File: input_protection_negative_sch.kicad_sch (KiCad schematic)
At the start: 23 parts, among them Q4 SQM50020EL, Q6 SQM50020EL, Q7 MMBT3904

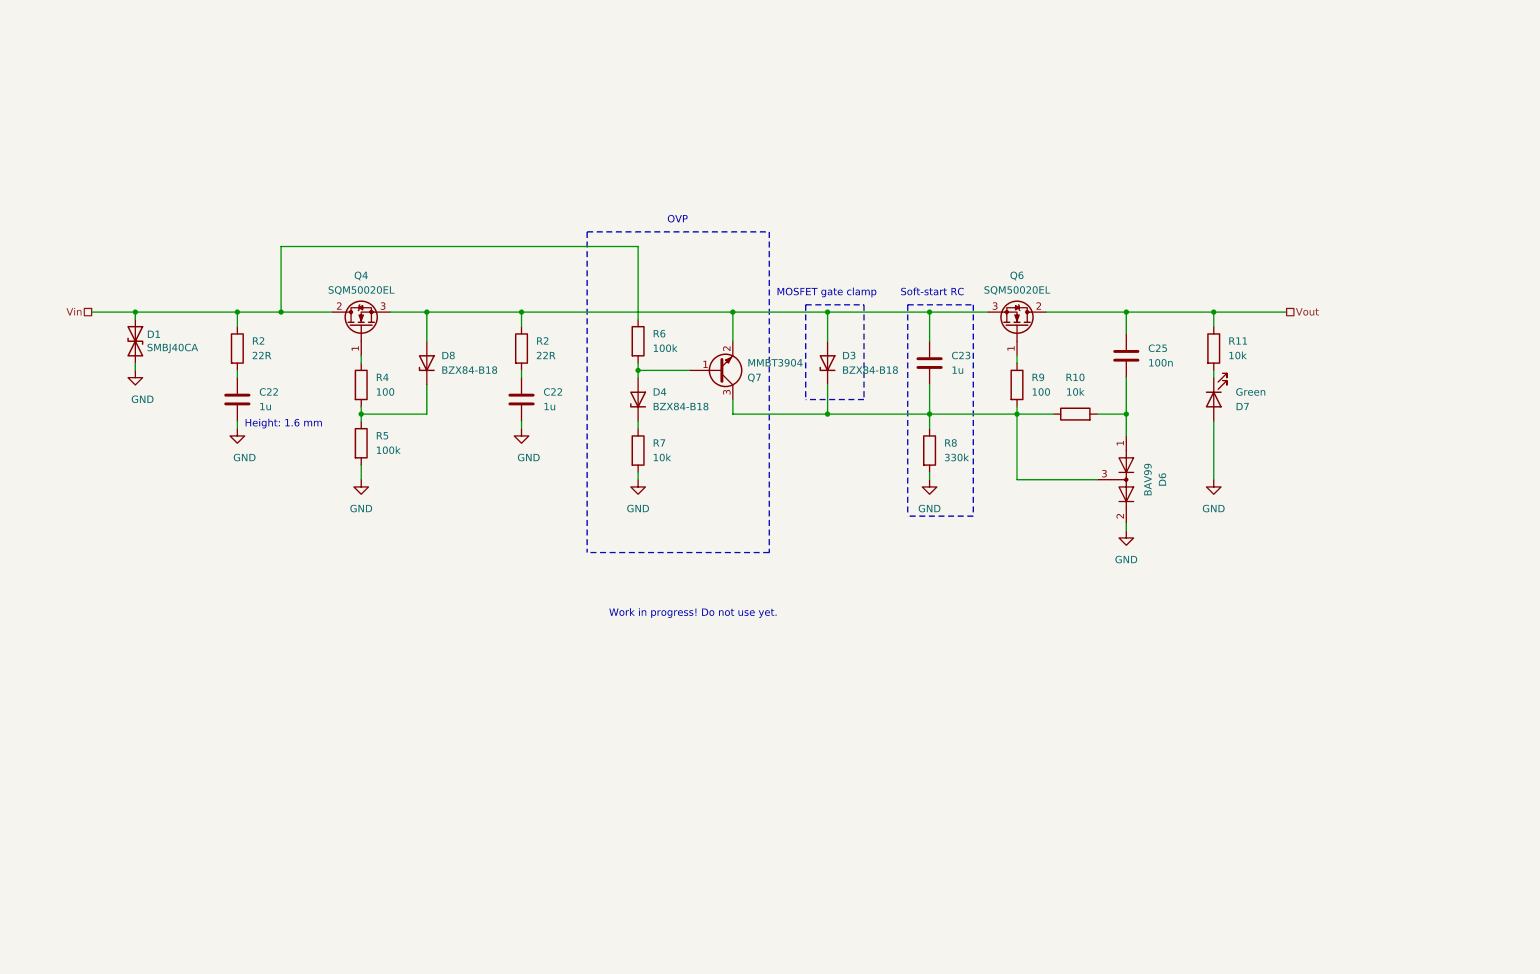
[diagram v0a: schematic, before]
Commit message: Added an input protection circuit Added CI
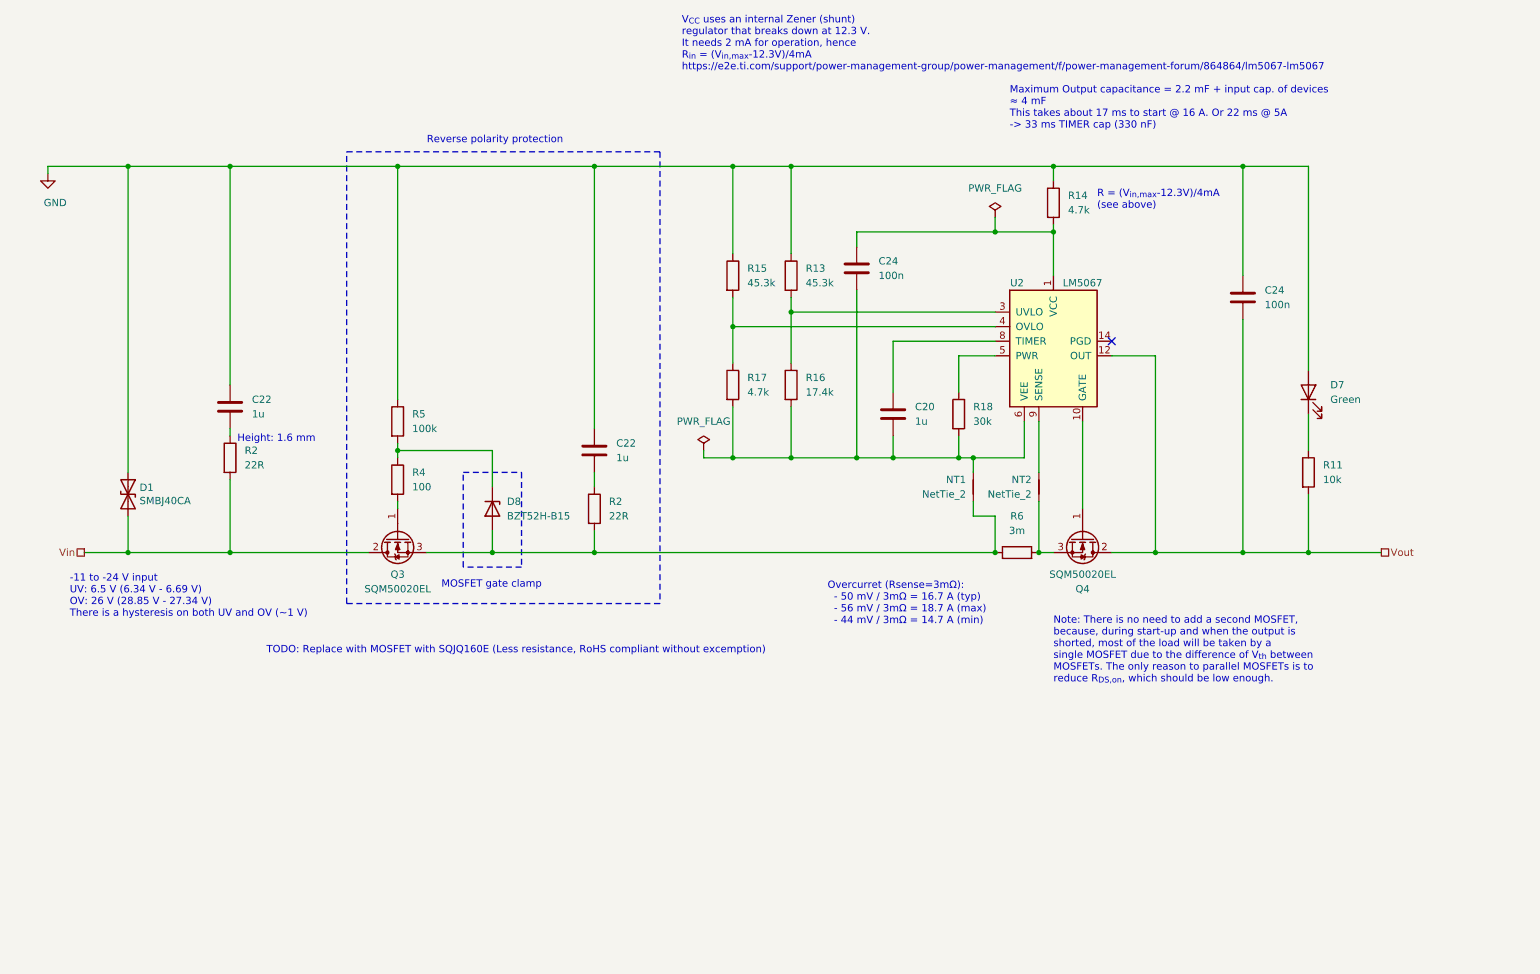
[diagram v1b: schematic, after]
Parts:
- removed C23: 1u, Capacitor_SMD:C_1206_3216Metric, symbol Device:C
- removed C25: 100n, Capacitor_SMD:C_1206_3216Metric, symbol Device:C
- removed D3, D4: BZX84-B18, Package_TO_SOT_SMD:SOT-23, symbol Diode:BZX84Cxx
- removed D6: BAV99, Package_TO_SOT_SMD:SOT-23, symbol Diode:BAV99
- removed Q7: MMBT3904, Package_TO_SOT_SMD:SOT-23, symbol Transistor_BJT:MMBT3904
- removed R10, R7: 10k, Resistor_SMD:R_0805_2012Metric, symbol Device:R
- removed R8: 330k, Resistor_SMD:R_0805_2012Metric, symbol Device:R
- removed R9: 100, Resistor_SMD:R_0805_2012Metric, symbol Device:R
- added C20: 1u, Capacitor_SMD:C_1206_3216Metric, symbol Device:C
- added C24 (x2): 100n, Capacitor_SMD:C_0805_2012Metric, symbol Device:C
- added NT1: NetTie_2, NetTie:NetTie-2_SMD_Pad0.5mm, symbol Device:NetTie_2
- added NT2: NetTie_2, Custom_footprints:NET-TIE-0.20mm, symbol Device:NetTie_2
- added R13, R15: 45.3k, Resistor_SMD:R_0805_2012Metric, symbol Device:R
- added R14, R17: 4.7k, Resistor_SMD:R_0805_2012Metric, symbol Device:R
- added R16: 17.4k, Resistor_SMD:R_0805_2012Metric, symbol Device:R
- added R18: 30k, Resistor_SMD:R_0805_2012Metric, symbol Device:R
- added U2: LM5067, Package_SO:SOIC-14_3.9x8.7mm_P1.27mm, symbol Texas Instruments:LM5067
- C22: RoHS (none) -> Yes; Temperature (none) -> Tstorage = –55 °C to 155 °C; digikey# (none) -> 399-13374-1-ND
- D1: MFN Bourns -> Littlefuse; PN SMBJ40CA-QH -> SZ1SMB40CAT3G; RoHS (none) -> Yes; Temperature (none) -> Tstorage = –55 °C to 150 °C
- D7: MFN Kingbright -> Osram; PN APT1608SGC -> LG L29K-G2J1-24; RoHS (none) -> Yes; Temperature (none) -> Tstorage = –40 °C to 100 °C
- D8: value BZX84-B18 -> BZT52H-B15; footprint Package_TO_SOT_SMD:SOT-23 -> Diode_SMD:D_SOD-123F; symbol Diode:BZX84Cxx -> Diode:BZT52Bxx; PN BZX84-B18,215 -> BZT52H-B15\,115; RoHS (none) -> Yes; Temperature (none) -> Tstorage = –65 °C to 150 °C; digikey# (none) -> 1727-1598-1-ND
- Q3: renamed from Q4; Note (none) -> Vds >= 60V; RoHS (none) -> By exemption; Temperature (none) -> Tstorage = –75 °C to 175 °C
- Q4: renamed from Q6; Note (none) -> Vds >= 60V; RoHS (none) -> By exemption; Temperature (none) -> Tstorage = –75 °C to 175 °C
- R11, R4, R5: Note (none) -> 1%, 150 V; RoHS (none) -> By exemption; Temperature (none) -> Tstorage = –55 °C to 155 °C
- R2: RoHS (none) -> By exemption; Temperature (none) -> Tstorage = –55 °C to 155 °C
- R6: value 100k -> 3m; footprint Resistor_SMD:R_0805_2012Metric -> Resistor_SMD:R_2512_6332Metric; MFN Vishay -> Bourns; PN CRCW0805100KFKEA -> CRE2512-FZ-R003E-3; RoHS (none) -> By exemption; Temperature (none) -> Tstorage = –75 °C to 170 °C
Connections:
- net GND: now also C22.1, C22.1, D1.1 (A1), R5.1, C24.1, R13.1, R14.1, R15.1; no longer C22.2, C22.2, D1.2 (A2), R5.2
- net Vin: now also D1.2 (A2), R2.2; no longer D1.1 (A1), R2.1, R6.1
- net Vout: now also R11.2, C24.2, U2.12 (OUT); no longer R11.1
- net at Q4.1 (G): now also U2.10 (GATE)
- net at D8.2 (A): now also Q3.3 (S), R2.2, R6.1, NT1.1
- net at R6.2: now also Q4.3 (S), NT2.1
- net at R4.1: now also D8.1 (K), R5.2; no longer Q3.1 (G)
- net at D7.1 (K): now also R11.1; no longer R11.2
- new net: C22.2, R2.1 (x2)
- new net: R13.2, R16.1, U2.3 (UVLO)
- new net: C20.2, C24.2, NT1.2, R16.2, R17.2, R18.2, U2.6 (VEE)
- new net: R15.2, R17.1, U2.4 (OVLO)
- new net: C24.1, R14.2, U2.1 (VCC)
- new net: R18.1, U2.5 (PWR)
- new net: C20.1, U2.8 (TIMER)
- new net: NT2.2, U2.9 (SENSE)
- new net: Q3.1 (G), R4.2
- no-connect marks 0 -> 1
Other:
- note added: "-11 to -24 V input UV: 6.5 V (6.34 V - 6.69 V) OV: 26 V (28.85 V - 27.34 V) There is a hysteresis on both UV and OV (~1 V)"
- note added: "Maximum Output capacitance = 2.2 mF + input cap. of devices ≈ 4 mF This takes about 17 ms to start @ 16 A. Or 22 ms @ 5A -> 33 ms TIMER cap (330 nF)"
- note added: "Note: There is no need to add a second MOSFET, because, during start-up and when the output is shorted, most of the load will be taken by a single MOSFET due to the difference of V_{th} between MOSFETs. The only reason to parallel MOSFETs is to reduce R_{DS,on}, which should be low enough."
- note added: "Overcurret (Rsense=3mΩ): - 50 mV / 3mΩ = 16.7 A (typ) - 56 mV / 3mΩ = 18.7 A (max) - 44 mV / 3mΩ = 14.7 A (min)"
- note added: "R = (V_{in,max}-12.3V)/4mA (see above)"
- note added: "Reverse polarity protection"
- note added: "TODO: Replace with MOSFET with SQJQ160E (Less resistance, RoHS compliant without excemption)"
- note added: "V_{CC} uses an internal Zener (shunt) regulator that breaks down at 12.3 V. It needs 2 mA for operation, hence R_{in} = (V_{in,max}-12.3V)/4mA https://e2e.ti.com/support/power-management-group/power-management/f/power-management-forum/864864/lm5067-lm5067"
- note removed: "OVP"
- note removed: "Soft-start RC"
- note removed: "Work in progress! Do not use yet."
- title: (none) -> Negative rail input protection
- moved on the sheet: C22, D1, D7, D8, Q3, Q4, R11, R2, R4, R5

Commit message: Added Ferrite beads at the board input Moved power connector silkscreen labels Added TODO list for v.2.1.0
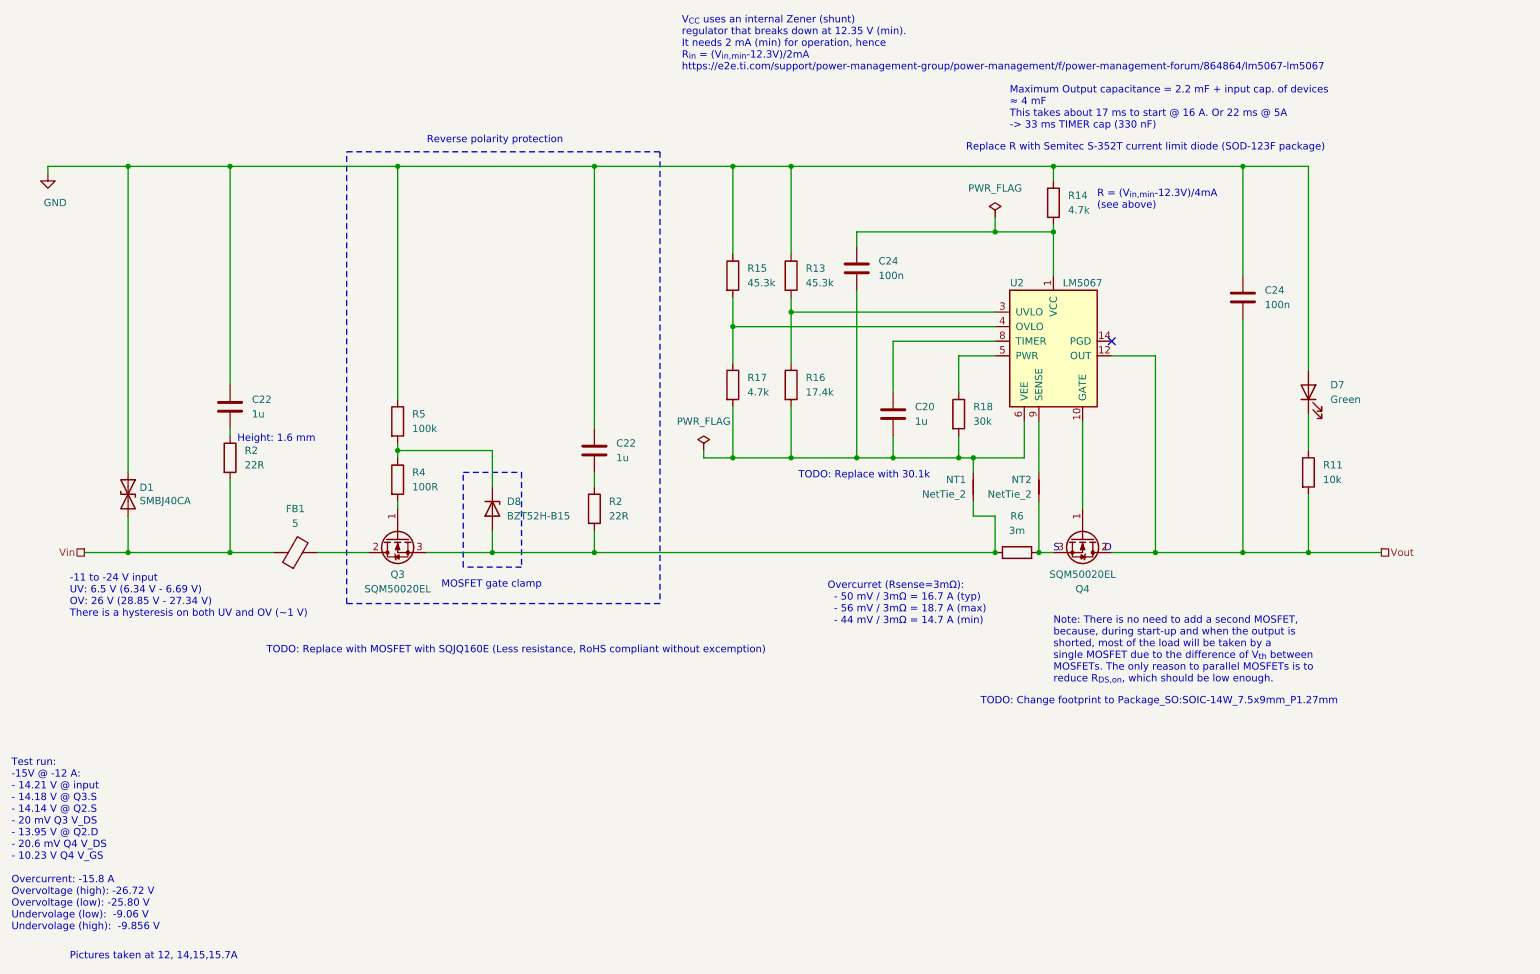
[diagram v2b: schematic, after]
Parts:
- added FB1: 5, Inductor_SMD:L_1210_3225Metric, symbol Device:FerriteBead
- R4: value 100 -> 100R
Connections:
- net Vin: now also FB1.1; no longer Q3.2 (D)
- new net: FB1.2, Q3.2 (D)
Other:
- note added: "D"
- note added: "Pictures taken at 12, 14,15,15.7A"
- note added: "R = (V_{in,min}-12.3V)/4mA (see above)"
- note added: "Replace R with Semitec S-352T current limit diode (SOD-123F package)"
- note added: "S"
- note added: "TODO: Change footprint to Package_SO:SOIC-14W_7.5x9mm_P1.27mm"
- note added: "TODO: Replace with 30.1k"
- note added: "Test run: -15V @ -12 A: - 14.21 V @ input - 14.18 V @ Q3.S - 14.14 V @ Q2.S - 20 mV Q3 V_DS - 13.95 V @ Q2.D - 20.6 mV Q4 V_DS - 10.23 V Q4 V_GS Overcurrent: -15.8 A Overvoltage (high): -26.72 V Overvoltage (low): -25.80 V Undervolage (low): -9.06 V Undervolage (high): -9.856 V"
- note added: "V_{CC} uses an internal Zener (shunt) regulator that breaks down at 12.35 V (min). It needs 2 mA (min) for operation, hence R_{in} = (V_{in,min}-12.3V)/2mA https://e2e.ti.com/support/power-management-group/power-management/f/power-management-forum/864864/lm5067-lm5067"
- note removed: "R = (V_{in,max}-12.3V)/4mA (see above)"
- note removed: "V_{CC} uses an internal Zener (shunt) regulator that breaks down at 12.3 V. It needs 2 mA for operation, hence R_{in} = (V_{in,max}-12.3V)/4mA https://e2e.ti.com/support/power-management-group/power-management/f/power-management-forum/864864/lm5067-lm5067"
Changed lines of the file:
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@@
-    (stroke (width 0) (type default))
-  )
-  (wire (pts (xy 64.77 106.68) (xy 88.9 106.68))
     (stroke (width 0) (type default))
   )
@@
     (stroke (width 0) (type default))
   )
+  (wire (pts (xy 64.77 106.68) (xy 72.39 106.68))
+    (stroke (width 0) (type default))
+  )
   (wire (pts (xy 46.99 106.68) (xy 64.77 106.68))
     (stroke (width 0) (type default))
@@
   )
   (wire (pts (xy 162.56 39.37) (xy 162.56 54.61))
+    (stroke (width 0) (type default))
+  )
+  (wire (pts (xy 80.01 106.68) (xy 88.9 106.68))
     (stroke (width 0) (type default))
   )
@@
     (effects (font (size 1.27 1.27)) (justify left bottom))
   )
+  (text "Replace R with Semitec S-352T current limit diode (SOD-123F package)"
+    (at 193.04 36.83 0)
+    (effects (font (size 1.27 1.27)) (justify left bottom))
+  )
+  (text "Pictures taken at 12, 14,15,15.7A" (at 36.83 177.8 0)
+    (effects (font (size 1.27 1.27)) (justify left bottom))
+  )
+  (text "S" (at 208.28 106.68 0)
+    (effects (font (size 1.27 1.27)) (justify left bottom))
+  )
+  (text "Test run:\n-15V @ -12 A:\n- 14.21 V @ input\n- 14.18 V @ Q3.S\n- 14.14 V @ Q2.S\n- 20 mV Q3 V_DS\n- 13.95 V @ Q2.D\n- 20.6 mV Q4 V_DS\n- 10.23 V Q4 V_GS\n\nOvercurrent: -15.8 A\nOvervoltage (high): -26.72 V\nOvervoltage (low): -25.80 V\nUndervolage (low):  -9.06 V\nUndervolage (high):  -9.856 V"
+    (at 26.67 172.72 0)
+    (effects (font (size 1.27 1.27)) (justify left bottom))
+  )
+  (text "TODO: Replace with 30.1k" (at 163.83 93.98 0)
+    (effects (font (size 1.27 1.27)) (justify left bottom))
+  )
   (text "Height: 1.6 mm" (at 66.04 87.63 0)
     (effects (font (size 1.27 1.27)) (justify left bottom))
+  )
+  (text "D" (at 218.44 106.68 0)
+    (effects (font (size 1.27 1.27)) (justify right bottom))
   )
   (text "TODO: Replace with MOSFET with SQJQ160E (Less resistance, RoHS compliant without excemption)"
@@
     (effects (font (size 1.27 1.27)) (justify left bottom))
   )
+  (text "TODO: Change footprint to Package_SO:SOIC-14W_7.5x9mm_P1.27mm"
+    (at 195.58 133.35 0)
+    (effects (font (size 1.27 1.27)) (justify left bottom))
+  )
   (text "Maximum Output capacitance = 2.2 mF + input cap. of devices\n≈ 4 mF\nThis takes about 17 ms to start @ 16 A. Or 22 ms @ 5A\n-> 33 ms TIMER cap (330 nF)"
     (at 200.66 33.02 0)
     (effects (font (size 1.27 1.27)) (justify left bottom))
   )
-  (text "V_{CC} uses an internal Zener (shunt)\nregulator that breaks down at 12.3 V.\nIt needs 2 mA for operation, hence\nR_{in} = (V_{in,max}-12.3V)/4mA\nhttps://e2e.ti.com/support/power-management-group/power-management/f/power-management-forum/864864/lm5067-lm5067\n"
+  (text "V_{CC} uses an internal Zener (shunt)\nregulator that breaks down at 12.35 V (min).\nIt needs 2 mA (min) for operation, hence\nR_{in} = (V_{in,min}-12.3V)/2mA\nhttps://e2e.ti.com/support/power-management-group/power-management/f/power-management-forum/864864/lm5067-lm5067\n"
     (at 143.51 22.86 0)
     (effects (font (size 1.27 1.27)) (justify left bottom))
@@
     (effects (font (size 1.27 1.27)) (justify left bottom))
   )
-  (text "R = (V_{in,max}-12.3V)/4mA\n(see above)" (at 215.9 46.99 0)
+  (text "R = (V_{in,min}-12.3V)/4mA\n(see above)" (at 215.9 46.99 0)
     (effects (font (size 1.27 1.27)) (justify left bottom))
   )
@@
         (path "/b4ace06a-3ad4-479e-aaa4-d547ecf6903f/1acfc0a8-4adc-455e-9f2b-420811df0901"
           (reference "R20") (unit 1)
+        )
+      )
+    )
+  )
+  (symbol (lib_id "Device:FerriteBead") (at 76.2 106.68 90) (unit 1)
+    (in_bom yes) (on_board yes) (dnp no) (fields_autoplaced)
+    (property "Reference" "FB1" (at 76.1492 99.06 90)
+      (effects (font (size 1.27 1.27)))
+    )
+    (property "Value" "5" (at 76.1492 101.6 90)
+      (effects (font (size 1.27 1.27)))
+    )
+    (property "Footprint" "Inductor_SMD:L_1210_3225Metric" (at 76.2 108.458 90)
+      (effects (font (size 1.27 1.27)) hide)
+    )
+    (property "Datasheet" "~" (at 76.2 106.68 0)
+      (effects (font (size 1.27 1.27)) hide)
+    )
+    (property "MFN" "Murata" (at 76.2 106.68 0)
+      (effects (font (size 1.27 1.27)) hide)
+    )
+    (property "PN" "BLE32SN120BH1L" (at 76.2 106.68 0)
+      (effects (font (size 1.27 1.27)) hide)
+    )
+    (property "Alternative" "Murata BLE32SN120SH1L" (at 76.2 106.68 90)
+      (effects (font (size 1.27 1.27)) hide)
+    )
+    (property "Temperature" "Tstorage = –55 °C to 150 °C" (at 76.2 106.68 0)
+      (effects (font (size 1.27 1.27)) hide)
+    )
+    (property "RoHS" "Yes" (at 76.2 106.68 0)
+      (effects (font (size 1.27 1.27)) hide)
+    )
+    (pin "1")
+    (pin "2")
+    (instances
+      (project "main"
+        (path "/b4ace06a-3ad4-479e-aaa4-d547ecf6903f/1acfc0a8-4adc-455e-9f2b-420811df0901"
+          (reference "FB1") (unit 1)
         )
       )
@@
       (effects (font (size 1.27 1.27)) (justify left))
     )
-    (property "Value" "100" (at 96.52 95.25 0)
-      (effects (font (size 1.27 1.27)) (justify left))
-    )
+    (property "Value" "100R" (at 96.52 95.25 0)
+      (effects (font (size 1.27 1.27)) (justify left))
+    )
